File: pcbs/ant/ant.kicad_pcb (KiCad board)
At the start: 2 copper layers, 106.7 x 80.9 mm, 17 parts, among them SW1 SW_PUSH, SW10 SW_PUSH, SW11 SW_PUSH, SW12 SW_PUSH, SW13 SW_PUSH, SW14 SW_PUSH, SW2 SW_PUSH, SW3 SW_PUSH, SW4 SW_PUSH, SW5 SW_PUSH, SW6 SW_PUSH, SW7 SW_PUSH, SW8 SW_PUSH, SW9 SW_PUSH, U1 ProMicro

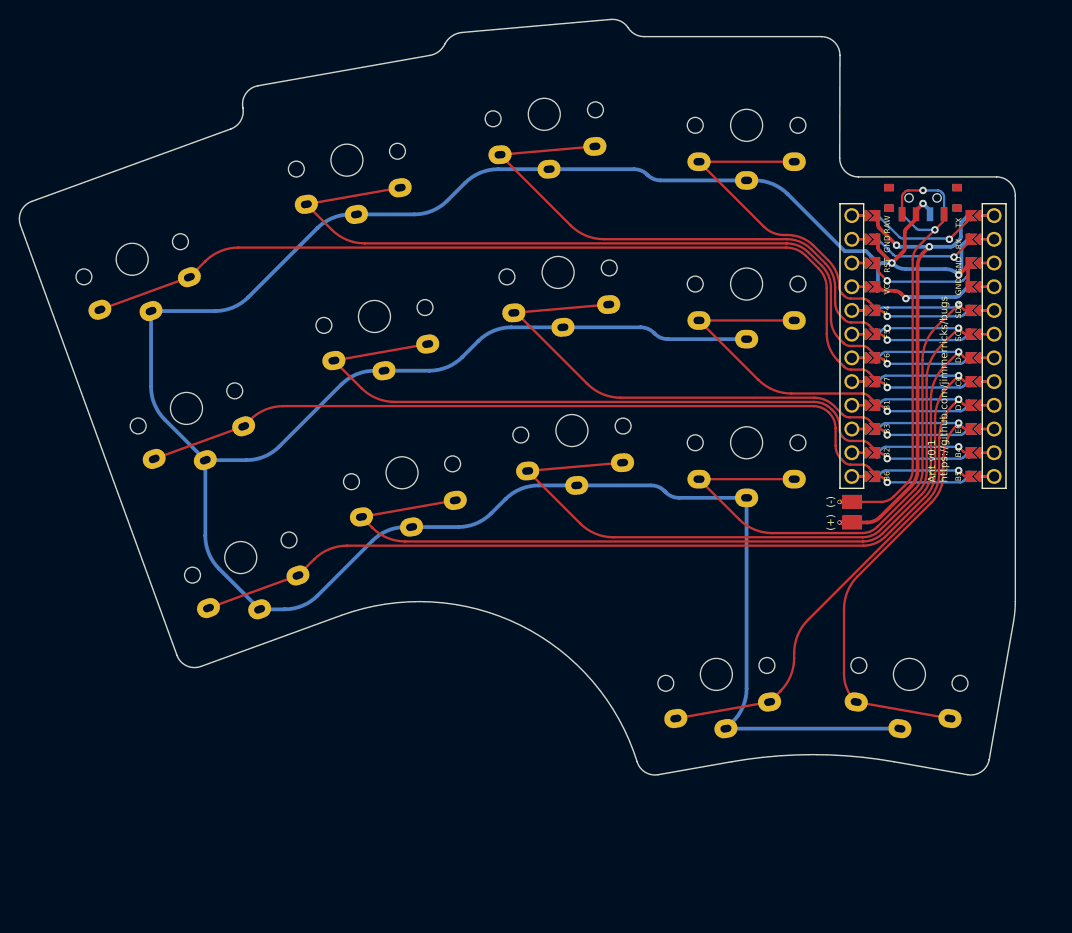
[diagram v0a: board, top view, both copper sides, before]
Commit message: Dropped a key from the Ant.
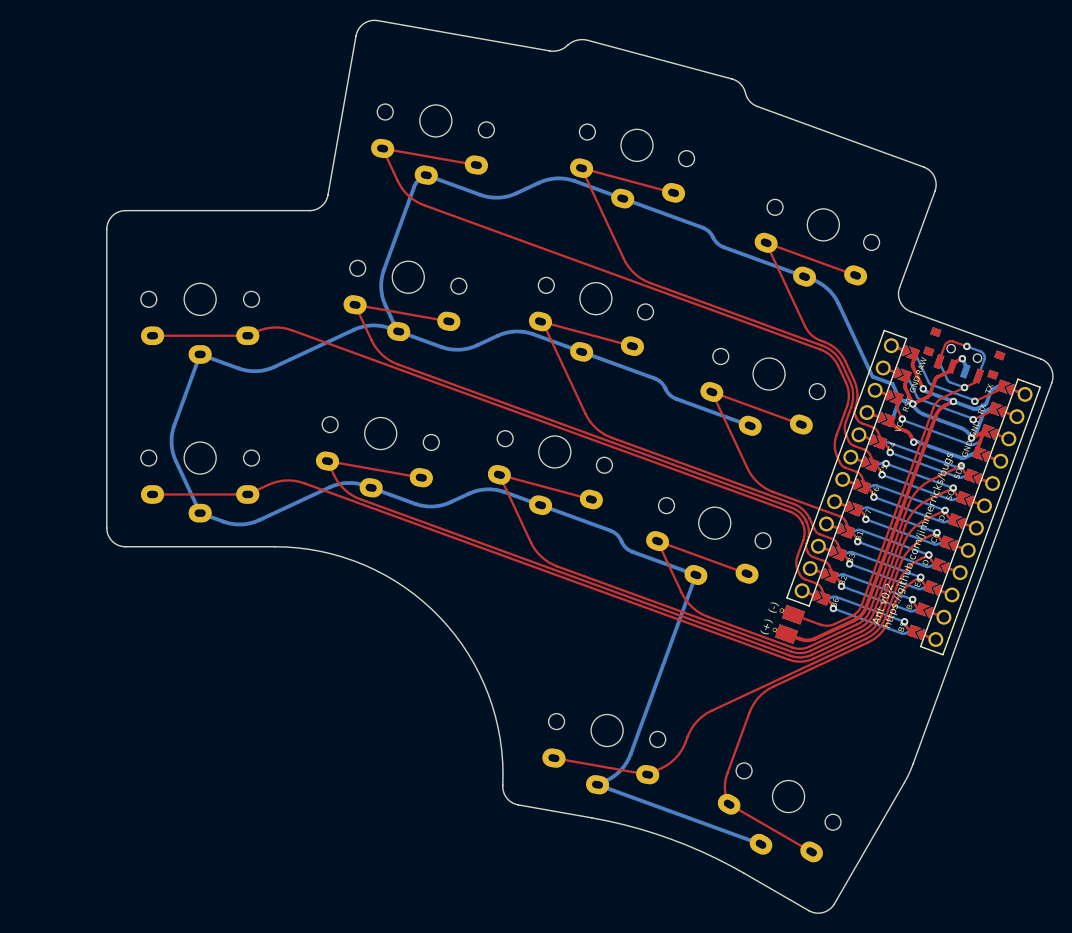
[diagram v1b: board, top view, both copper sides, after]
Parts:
- removed the SW1 at (36.7, 86.1)
- moved SW13 18.4 mm to (107.0, 143.7), turned to -30 degrees
- moved PSW1 17.2 mm to (125.8, 96.2), turned to 160 degrees
- moved U1 15.7 mm to (120.4, 111.1), turned to -20 degrees
- moved BT1 13.7 mm to (107.2, 125.3), turned to 70 degrees
- moved SW3 13.5 mm to (110.7, 82.5), turned to -20 degrees
- moved SW12 13.2 mm to (87.6, 136.6), turned to -10 degrees
- moved SW4 11.8 mm to (44.0, 90.4), turned to 0 degrees
- moved SW8 11.5 mm to (44.0, 107.4), turned to 0 degrees
- moved SW2 10.5 mm to (90.8, 73.9), turned to -15 degrees
- moved SW1 10.4 mm to (69.2, 71.3), turned to -10 degrees
- moved SW7 9.93 mm to (104.9, 98.4), turned to -20 degrees
- moved SW11 9.26 mm to (99.1, 114.4), turned to -20 degrees
- moved SW5 5.55 mm to (66.3, 88.1), turned to -10 degrees
- moved SW6 4.93 mm to (86.4, 90.4), turned to -15 degrees
- moved SW9 4.78 mm to (63.3, 104.8), turned to -10 degrees
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- renumbered SW2 to SW1, SW11 to SW10, SW12 to SW11, SW13 to SW12, SW14 to SW13, SW3 to SW2, SW4 to SW3, SW5 to SW4, SW6 to SW5, SW7 to SW6, SW8 to SW7, SW9 to SW8, SW10 to SW9
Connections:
- SW1 pad 1: switch2 -> switch1
- SW10 pad 1: switch11 -> switch10
- SW11 pad 1: switch12 -> switch11
- SW12 pad 1: switch13 -> switch12
- SW13 pad 1: switch14 -> switch13
- SW2 pad 1: switch3 -> switch2
- SW3 pad 1: switch4 -> switch3
- SW4 pad 1: switch5 -> switch4
- SW5 pad 1: switch6 -> switch5
- SW6 pad 1: switch7 -> switch6
- SW7 pad 1: switch8 -> switch7
- SW8 pad 1: switch9 -> switch8
- SW9 pad 1: switch10 -> switch9
- U1 pad 10: switch14 -> switch13
- U1 pad 13: switch5 -> switch4
- U1 pad 14: switch6 -> switch5
- U1 pad 15: switch7 -> switch6
- U1 pad 16: switch8 -> switch7
- U1 pad 17: switch1 -> unconnected-(U1-Pad17)
- U1 pad 18: switch2 -> switch1
- U1 pad 19: switch3 -> switch2
- U1 pad 20: switch4 -> switch3
- U1 pad 5: switch12 -> switch11
- U1 pad 6: switch11 -> switch10
- U1 pad 7: switch10 -> switch9
- U1 pad 8: switch9 -> switch8
- U1 pad 9: switch13 -> switch12
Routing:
- net switch8: track 43.0 -> 104.6 mm
- net switch14: track 54.9 -> 0.00 mm, vias 1 -> 0
- net switch4: track 46.6 -> 93.8 mm
- net GND: track 319.4 -> 294.5 mm
- net switch3: track 70.3 -> 46.6 mm
- net switch7: track 64.0 -> 43.0 mm
- net switch2: track 91.0 -> 70.3 mm
- net switch6: track 83.1 -> 64.0 mm
- net switch11: track 85.7 -> 68.8 mm, vias 2 -> 1
- net switch1: track 105.1 -> 91.0 mm
- net switch10: track 99.6 -> 85.7 mm, vias 1 -> 2
- net switch5: track 93.8 -> 83.1 mm
- net unconnected-(U1-Pad17): track 0.00 -> 10.1 mm, vias 0 -> 1
- net switch12: track 68.8 -> 60.2 mm
- net switch13: track 60.2 -> 54.9 mm
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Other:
- board size 106.7 x 80.9 mm -> 101.3 x 95.6 mm
- board text added: "Ant v0.2 https://github.com/jimmerricks/bugs"
- board text removed: "Ant v0.1 https://github.com/jimmerricks/bugs"

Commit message: Minor edits
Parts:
- moved SW4 13.6 mm to (39.0, 103.1), turned to 15 degrees
- moved SW1 12.7 mm to (58.5, 78.1), turned to 5 degrees
- moved SW8 12.1 mm to (43.4, 119.5), turned to 15 degrees
- moved SW2 10.9 mm to (80.0, 75.1), turned to 0 degrees
- moved PSW1 10.7 mm to (119.6, 87.5), turned to 175 degrees
- moved SW3 10.2 mm to (101.5, 78.1), turned to -5 degrees
- moved SW5 9.41 mm to (60.0, 95.0), turned to 5 degrees
- moved SW13 8.64 mm to (113.7, 138.2), turned to -15 degrees
- moved U1 8.11 mm to (118.2, 103.3), turned to -5 degrees
- moved SW9 7.42 mm to (61.5, 112.0), turned to 5 degrees
- moved SW6 6.63 mm to (80.0, 92.1), turned to 0 degrees
- moved SW7 5.99 mm to (100.0, 95.1), turned to -5 degrees
- moved SW12 5.53 mm to (93.1, 136.4), turned to 5 degrees
- moved BT1 5.23 mm to (109.1, 120.4), turned to 85 degrees
- moved SW10 3.04 mm to (80.0, 109.1), turned to 0 degrees
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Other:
- board size 101.3 x 95.6 mm -> 102.1 x 84 mm
